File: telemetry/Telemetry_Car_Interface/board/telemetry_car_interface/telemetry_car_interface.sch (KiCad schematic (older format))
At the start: 38 parts, among them J1 CONN_02X03, U1 MCP2561-E_SN, U101 TPS560430YF, U2 ATMEGA16M1, Y1 Crystal_SMD

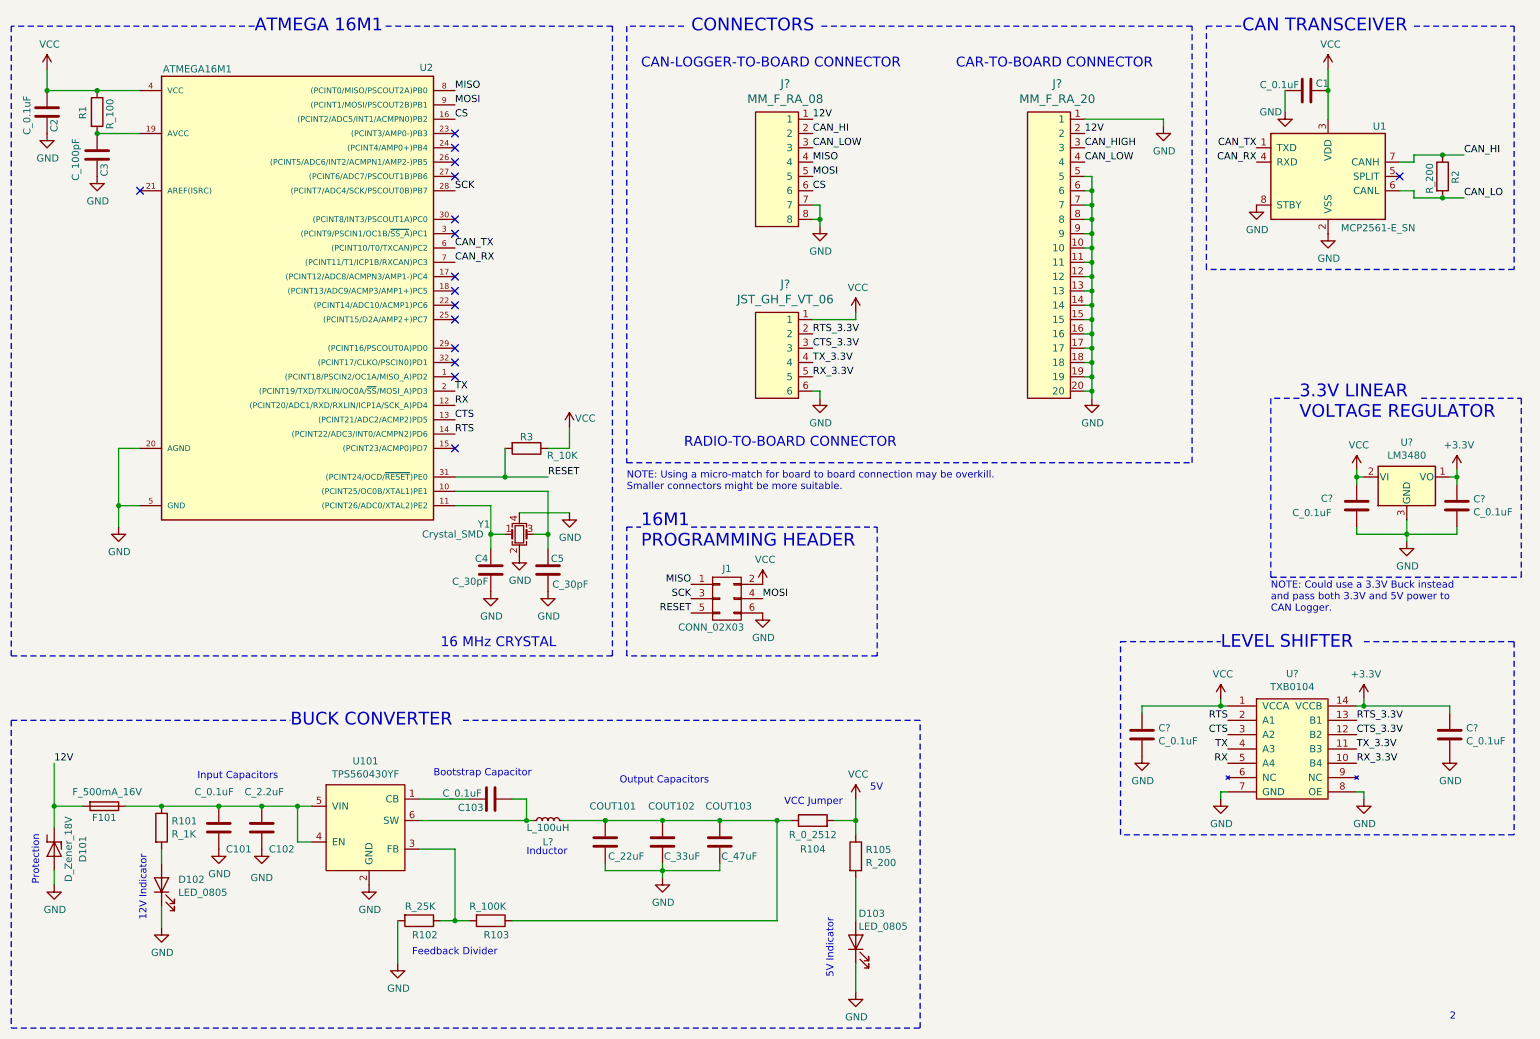
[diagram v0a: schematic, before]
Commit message: Fix buck converter, CAN transceiver and net labels
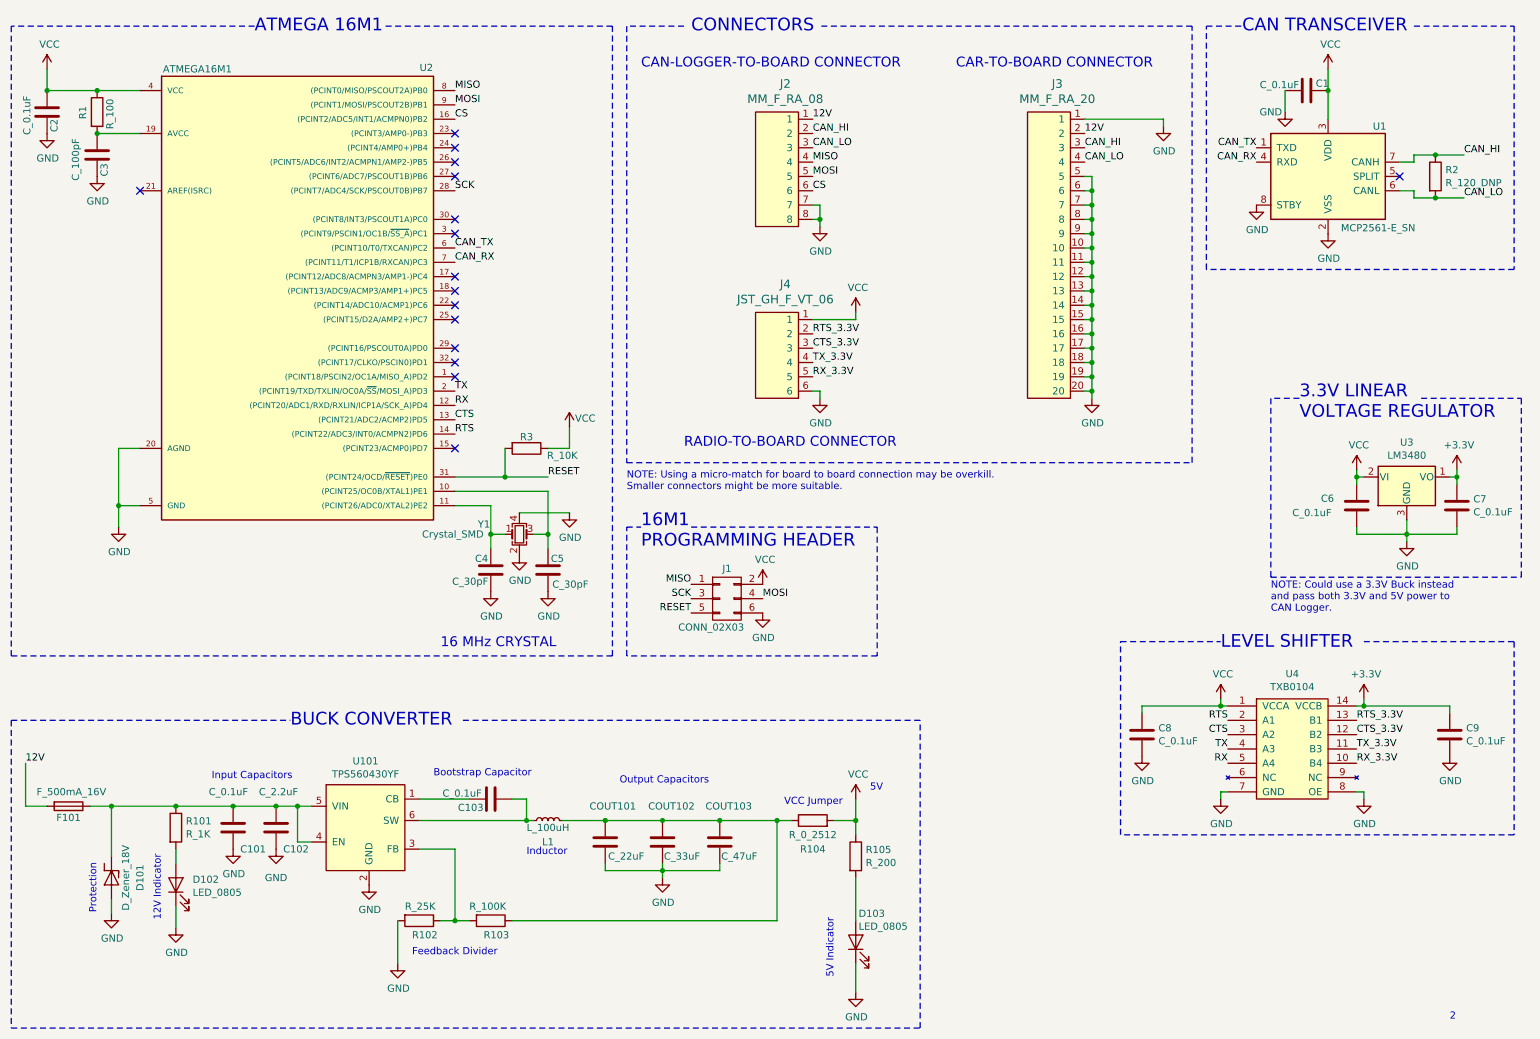
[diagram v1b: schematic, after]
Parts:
- removed R2: R_200, footprints:R_0805_OEM, symbol template-rescue:R_200-formula
- added R2: R_120_DNP, footprints:R_0805_OEM, symbol formula:R_120_DNP
- gave numbers to parts that had none: 10
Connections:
- net CAN_HIGH is gone; now on net CAN_HI: J3.3
- net CAN_LOW is gone; now on net CAN_LO: J2.3, J3.4
- net 12V: no longer D101.1 (K)
- net CAN_HI: now also R2.1
- net CAN_LO: now also R2.2
- net at C101.1, C102.1, F101.1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: now also D101.1 (K)
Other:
- moved on the sheet: C101, C102, D101, D102, F101, R101
